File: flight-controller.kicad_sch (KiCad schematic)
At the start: 13 parts, among them J1 Conn_02x10_Odd_Even, J2 Conn_02x08_Odd_Even, J3 Conn_02x17_Odd_Even, J4 Conn_02x15_Counter_Clockwise, J5 Conn_01x02, U3 ACS773LCB-100B-PFF-T

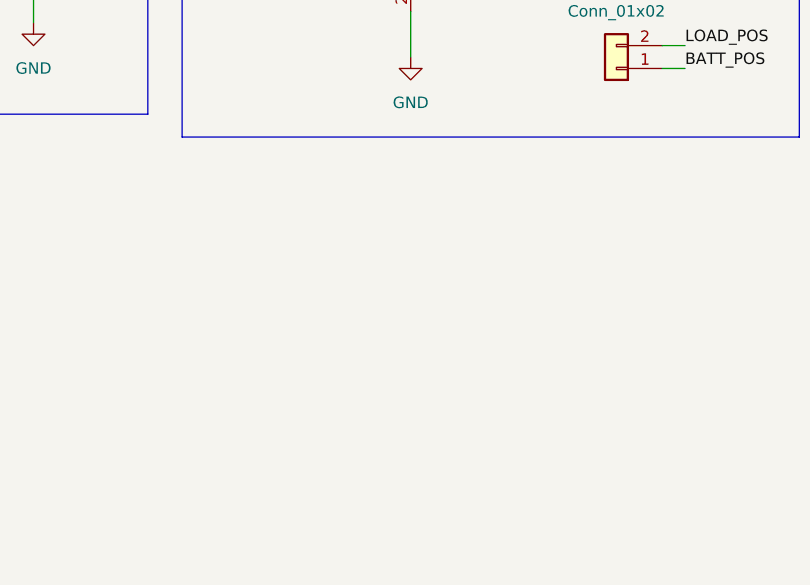
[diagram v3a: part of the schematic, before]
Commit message: feat: Added pinout of BN-088
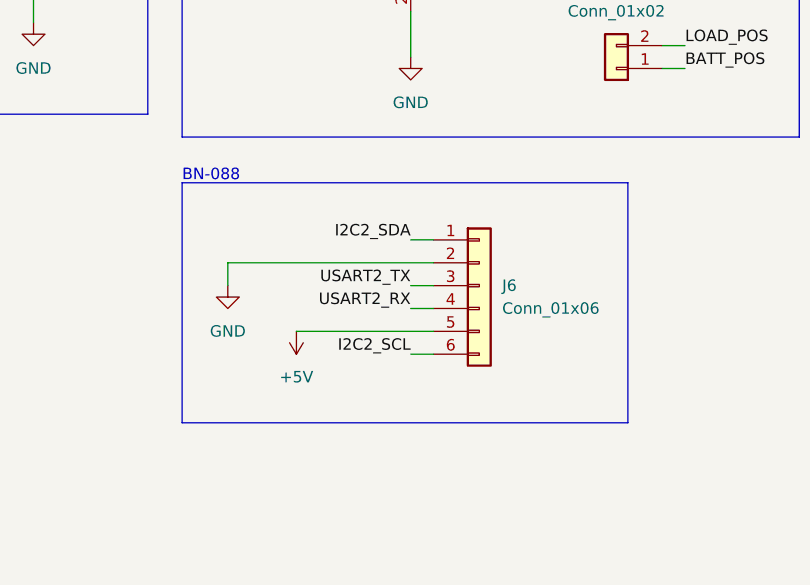
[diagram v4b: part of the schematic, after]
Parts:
- added J6: Conn_01x06, symbol Connector_Generic:Conn_01x06
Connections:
- net GND: now also J6.2 (Pin_2)
- new net +5V: J6.5 (Pin_5)
- new net I2C2_SCL: J6.6 (Pin_6)
- new net I2C2_SDA: J6.1 (Pin_1)
- new net USART2_RX: J6.4 (Pin_4)
- new net USART2_TX: J6.3 (Pin_3)
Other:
- note added: "BN-088"
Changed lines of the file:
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@@
+    (stroke (width 0) (type default))
+  )
+  (wire (pts (xy 219.71 88.9) (xy 222.25 88.9))
     (stroke (width 0) (type default))
   )
@@
     (stroke (width 0) (type default))
   )
+  (wire (pts (xy 219.71 93.98) (xy 222.25 93.98))
+    (stroke (width 0) (type default))
+  )
   (wire (pts (xy 148.59 48.26) (xy 153.67 48.26))
     (stroke (width 0) (type default))
@@
     (stroke (width 0) (type default))
   )
+  (wire (pts (xy 199.39 86.36) (xy 199.39 83.82))
+    (stroke (width 0) (type default))
+  )
   (wire (pts (xy 60.96 52.07) (xy 63.5 52.07))
     (stroke (width 0) (type default))
@@
     (stroke (width 0) (type default))
   )
+  (wire (pts (xy 207.01 91.44) (xy 222.25 91.44))
+    (stroke (width 0) (type default))
+  )
   (wire (pts (xy 63.5 52.07) (xy 63.5 54.61))
     (stroke (width 0) (type default))
@@
     (stroke (width 0) (type default))
   )
+  (wire (pts (xy 219.71 81.28) (xy 222.25 81.28))
+    (stroke (width 0) (type default))
+  )
   (wire (pts (xy 165.1 33.02) (xy 165.1 38.1))
     (stroke (width 0) (type default))
@@
     (stroke (width 0) (type default))
   )
+  (wire (pts (xy 199.39 83.82) (xy 222.25 83.82))
+    (stroke (width 0) (type default))
+  )
   (wire (pts (xy 93.98 49.53) (xy 93.98 53.34))
     (stroke (width 0) (type default))
@@
     (stroke (width 0) (type default))
   )
+  (wire (pts (xy 219.71 86.36) (xy 222.25 86.36))
+    (stroke (width 0) (type default))
+  )
   (wire (pts (xy 81.28 49.53) (xy 81.28 53.34))
     (stroke (width 0) (type default))
@@
     (fill (type none))
   )
+  (rectangle (start 194.31 74.93) (end 243.84 101.6)
+    (stroke (width 0) (type default))
+    (fill (type none))
+  )
   (text "ACS773" (at 194.31 24.13 0)
     (effects (font (size 1.27 1.27)) (justify left bottom))
@@
     (effects (font (size 1.27 1.27)) (justify left bottom))
   )
+  (text "BN-088" (at 194.31 74.93 0)
+    (effects (font (size 1.27 1.27)) (justify left bottom))
+  )
   (text "BMP390" (at 110.49 24.13 0)
     (effects (font (size 1.27 1.27)) (justify left bottom))
@@
     (effects (font (size 1.27 1.27)) (justify left bottom))
   )
+  (label "I2C2_SCL" (at 219.71 93.98 180) (fields_autoplaced)
+    (effects (font (size 1.27 1.27)) (justify right bottom))
+  )
   (label "LOAD_POS" (at 207.01 50.8 180) (fields_autoplaced)
     (effects (font (size 1.27 1.27)) (justify right bottom))
   )
+  (label "USART2_TX" (at 219.71 86.36 180) (fields_autoplaced)
+    (effects (font (size 1.27 1.27)) (justify right bottom))
+  )
   (label "SPI4_MISO" (at 125.73 43.18 180) (fields_autoplaced)
     (effects (font (size 1.27 1.27)) (justify right bottom))
@@
     (effects (font (size 1.27 1.27)) (justify right bottom))
   )
+  (label "USART2_RX" (at 219.71 88.9 180) (fields_autoplaced)
+    (effects (font (size 1.27 1.27)) (justify right bottom))
+  )
   (label "SPI1_CS_GYRO" (at 62.23 48.26 0) (fields_autoplaced)
     (effects (font (size 1.27 1.27)) (justify left bottom))
@@
   (label "SPI1_SCK" (at 62.23 40.64 0) (fields_autoplaced)
     (effects (font (size 1.27 1.27)) (justify left bottom))
+  )
+  (label "I2C2_SDA" (at 219.71 81.28 180) (fields_autoplaced)
+    (effects (font (size 1.27 1.27)) (justify right bottom))
   )
   (label "SPI1_MISO" (at 34.29 36.83 180) (fields_autoplaced)
@@
     )
   )
+  (symbol (lib_id "Connector_Generic:Conn_01x06") (at 227.33 86.36 0) (unit 1)
+    (in_bom yes) (on_board yes) (dnp no) (fields_autoplaced)
+    (property "Reference" "J6" (at 229.87 86.36 0)
+      (effects (font (size 1.27 1.27)) (justify left))
+    )
+    (property "Value" "Conn_01x06" (at 229.87 88.9 0)
+      (effects (font (size 1.27 1.27)) (justify left))
+    )
+    (property "Footprint" "" (at 227.33 86.36 0)
+      (effects (font (size 1.27 1.27)) hide)
+    )
+    (property "Datasheet" "~" (at 227.33 86.36 0)
+      (effects (font (size 1.27 1.27)) hide)
+    )
+    (pin "3")
+    (pin "4")
+    (pin "6")
+    (pin "2")
+    (pin "5")
+    (pin "1")
+    (instances
+      (project "flight-controller"
+        (path "/1e8bc6c3-9c25-4744-8bc3-112c39d50b38"
+          (reference "J6") (unit 1)
+        )
+      )
+    )
+  )
   (symbol (lib_id "power:GND") (at 177.8 57.15 0) (unit 1)
     (in_bom yes) (on_board yes) (dnp no) (fields_autoplaced)
@@
     )
   )
+  (symbol (lib_id "power:GND") (at 199.39 86.36 0) (unit 1)
+    (in_bom yes) (on_board yes) (dnp no) (fields_autoplaced)
+    (property "Reference" "#PWR016" (at 199.39 92.71 0)
+      (effects (font (size 1.27 1.27)) hide)
+    )
+    (property "Value" "GND" (at 199.39 91.44 0)
+      (effects (font (size 1.27 1.27)))
+    )
+    (property "Footprint" "" (at 199.39 86.36 0)
+      (effects (font (size 1.27 1.27)) hide)
+    )
+    (property "Datasheet" "" (at 199.39 86.36 0)
+      (effects (font (size 1.27 1.27)) hide)
+    )
+    (pin "1")
+    (instances
+      (project "flight-controller"
+        (path "/1e8bc6c3-9c25-4744-8bc3-112c39d50b38"
+          (reference "#PWR016") (unit 1)
+        )
+      )
+    )
+  )
   (symbol (lib_id "power:+3.3V") (at 213.36 35.56 90) (unit 1)
     (in_bom yes) (on_board yes) (dnp no) (fields_autoplaced)
@@
         )
       )
+    )
+  )
+  (symbol (lib_id "power:+5V") (at 207.01 91.44 180) (unit 1)
+    (in_bom yes) (on_board yes) (dnp no) (fields_autoplaced)
+    (property "Reference" "#PWR017" (at 207.01 87.63 0)
+      (effects (font (size 1.27 1.27)) hide)
+    )
+    (property "Value" "+5V" (at 207.01 96.52 0)
+      (effects (font (size 1.27 1.27)))
+    )
+    (property "Footprint" "" (at 207.01 91.44 0)
+      (effects (font (size 1.27 1.27)) hide)
+    )
+    (property "Datasheet" "" (at 207.01 91.44 0)
+      (effects (font (size 1.27 1.27)) hide)
+    )
+    (pin "1")
+    (instances
+      (project "flight-controller"
+        (path "/1e8bc6c3-9c25-4744-8bc3-112c39d50b38"
+          (reference "#PWR017") (unit 1)
+        )
+      )

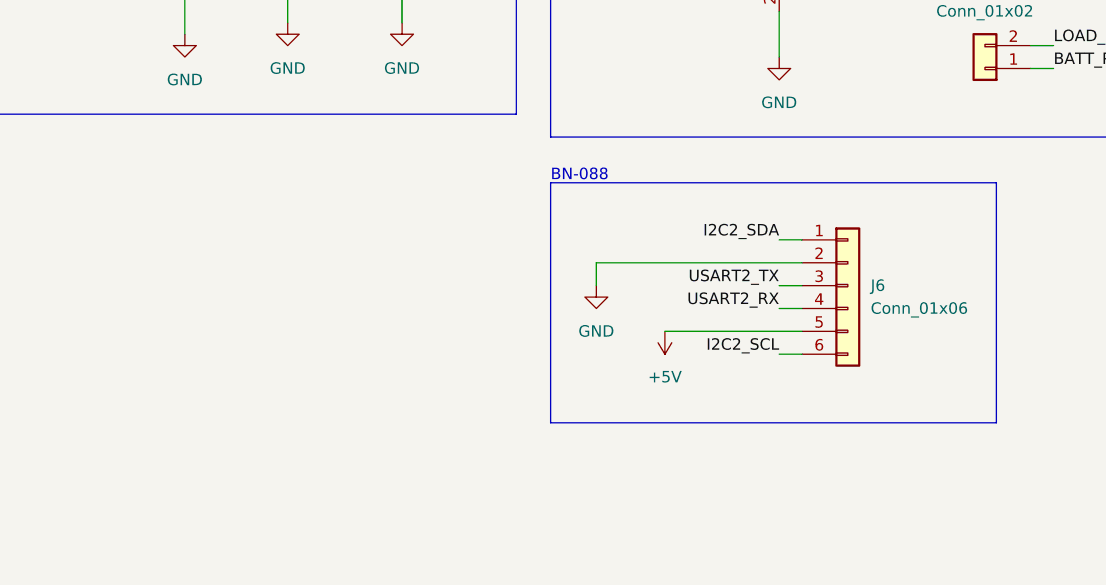
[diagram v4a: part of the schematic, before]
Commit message: feat: Added J_ESC_POWER pins for powering the board
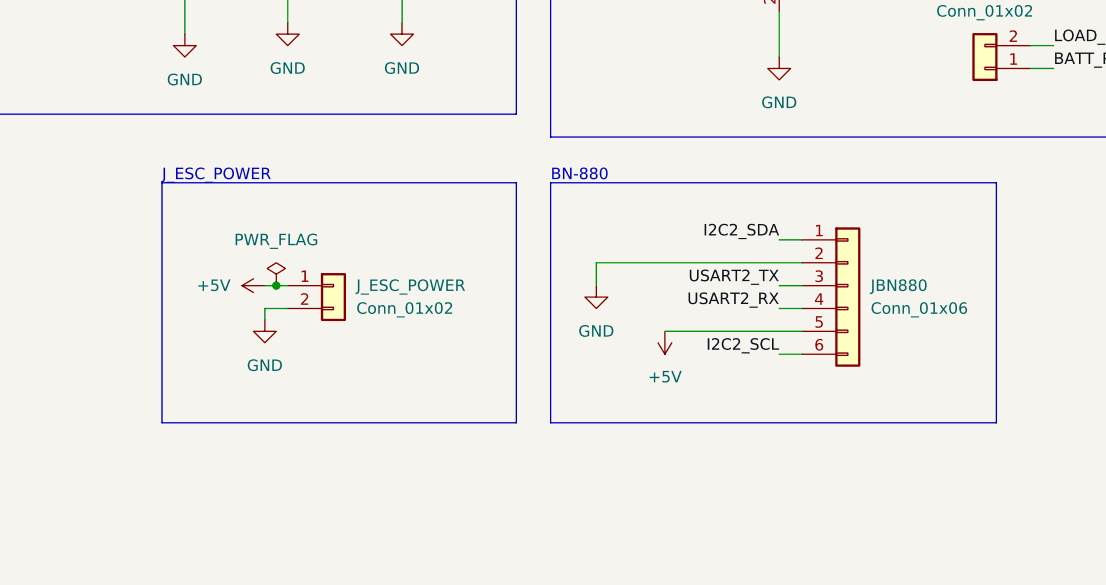
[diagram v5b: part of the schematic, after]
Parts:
- added J_ESC_POWER: Conn_01x02, symbol Connector_Generic:Conn_01x02
- renumbered J6 to JBN880
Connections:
- net +5V: now also J_ESC_POWER.1 (Pin_1)
- net GND: now also J_ESC_POWER.2 (Pin_2)
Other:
- note added: "BN-880"
- note added: "J_ESC_POWER"
- note removed: "BN-088"
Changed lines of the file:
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@@
   (junction (at 93.98 36.83) (diameter 0) (color 0 0 0 0)
+  )
+  (junction (at 163.83 86.36) (diameter 0) (color 0 0 0 0)
   )
   (junction (at 219.71 35.56) (diameter 0) (color 0 0 0 0)
@@
     (stroke (width 0) (type default))
   )
+  (wire (pts (xy 162.56 86.36) (xy 163.83 86.36))
+    (stroke (width 0) (type default))
+  )
   (wire (pts (xy 125.73 40.64) (xy 128.27 40.64))
     (stroke (width 0) (type default))
@@
     (stroke (width 0) (type default))
   )
+  (wire (pts (xy 163.83 86.36) (xy 165.1 86.36))
+    (stroke (width 0) (type default))
+  )
   (wire (pts (xy 247.65 62.23) (xy 250.19 62.23))
     (stroke (width 0) (type default))
@@
     (stroke (width 0) (type default))
   )
+  (wire (pts (xy 162.56 88.9) (xy 162.56 90.17))
+    (stroke (width 0) (type default))
+  )
+  (wire (pts (xy 165.1 88.9) (xy 162.56 88.9))
+    (stroke (width 0) (type default))
+  )
   (wire (pts (xy 93.98 31.75) (xy 93.98 36.83))
     (stroke (width 0) (type default))
@@
     (fill (type none))
   )
+  (rectangle (start 151.13 74.93) (end 190.5 101.6)
+    (stroke (width 0) (type default))
+    (fill (type none))
+  )
   (rectangle (start 110.49 24.13) (end 190.5 67.31)
     (stroke (width 0) (type default))
@@
     (effects (font (size 1.27 1.27)) (justify left bottom))
   )
+  (text "J_ESC_POWER" (at 151.13 74.93 0)
+    (effects (font (size 1.27 1.27)) (justify left bottom))
+  )
   (text "BMI088" (at 21.59 24.13 0)
     (effects (font (size 1.27 1.27)) (justify left bottom))
   )
-  (text "BN-088" (at 194.31 74.93 0)
+  (text "BN-880" (at 194.31 74.93 0)
     (effects (font (size 1.27 1.27)) (justify left bottom))
   )
@@
     )
   )
+  (symbol (lib_id "power:GND") (at 162.56 90.17 0) (unit 1)
+    (in_bom yes) (on_board yes) (dnp no) (fields_autoplaced)
+    (property "Reference" "#PWR018" (at 162.56 96.52 0)
+      (effects (font (size 1.27 1.27)) hide)
+    )
+    (property "Value" "GND" (at 162.56 95.25 0)
+      (effects (font (size 1.27 1.27)))
+    )
+    (property "Footprint" "" (at 162.56 90.17 0)
+      (effects (font (size 1.27 1.27)) hide)
+    )
+    (property "Datasheet" "" (at 162.56 90.17 0)
+      (effects (font (size 1.27 1.27)) hide)
+    )
+    (pin "1")
+    (instances
+      (project "flight-controller"
+        (path "/1e8bc6c3-9c25-4744-8bc3-112c39d50b38"
+          (reference "#PWR018") (unit 1)
+        )
+      )
+    )
+  )
   (symbol (lib_id "power:GND") (at 219.71 60.96 0) (unit 1)
     (in_bom yes) (on_board yes) (dnp no) (fields_autoplaced)
@@
   (symbol (lib_id "Connector_Generic:Conn_01x06") (at 227.33 86.36 0) (unit 1)
     (in_bom yes) (on_board yes) (dnp no) (fields_autoplaced)
-    (property "Reference" "J6" (at 229.87 86.36 0)
+    (property "Reference" "JBN880" (at 229.87 86.36 0)
       (effects (font (size 1.27 1.27)) (justify left))
     )
@@
       (project "flight-controller"
         (path "/1e8bc6c3-9c25-4744-8bc3-112c39d50b38"
-          (reference "J6") (unit 1)
+          (reference "JBN880") (unit 1)
         )
       )
@@
     )
   )
+  (symbol (lib_id "power:PWR_FLAG") (at 163.83 86.36 0) (unit 1)
+    (in_bom yes) (on_board yes) (dnp no) (fields_autoplaced)
+    (property "Reference" "#FLG01" (at 163.83 84.455 0)
+      (effects (font (size 1.27 1.27)) hide)
+    )
+    (property "Value" "PWR_FLAG" (at 163.83 81.28 0)
+      (effects (font (size 1.27 1.27)))
+    )
+    (property "Footprint" "" (at 163.83 86.36 0)
+      (effects (font (size 1.27 1.27)) hide)
+    )
+    (property "Datasheet" "~" (at 163.83 86.36 0)
+      (effects (font (size 1.27 1.27)) hide)
+    )
+    (pin "1")
+    (instances
+      (project "flight-controller"
+        (path "/1e8bc6c3-9c25-4744-8bc3-112c39d50b38"
+          (reference "#FLG01") (unit 1)
+        )
+      )
+    )
+  )
   (symbol (lib_id "power:+3.3V") (at 165.1 33.02 0) (unit 1)
     (in_bom yes) (on_board yes) (dnp no) (fields_autoplaced)
@@
     )
   )
+  (symbol (lib_id "power:+5V") (at 162.56 86.36 90) (unit 1)
+    (in_bom yes) (on_board yes) (dnp no) (fields_autoplaced)
+    (property "Reference" "#PWR019" (at 166.37 86.36 0)
+      (effects (font (size 1.27 1.27)) hide)
+    )
+    (property "Value" "+5V" (at 158.75 86.36 90)
+      (effects (font (size 1.27 1.27)) (justify left))
+    )
+    (property "Footprint" "" (at 162.56 86.36 0)
+      (effects (font (size 1.27 1.27)) hide)
+    )
+    (property "Datasheet" "" (at 162.56 86.36 0)
+      (effects (font (size 1.27 1.27)) hide)
+    )
+    (pin "1")
+    (instances
+      (project "flight-controller"
+        (path "/1e8bc6c3-9c25-4744-8bc3-112c39d50b38"
+          (reference "#PWR019") (unit 1)
+        )
+      )
+    )
+  )
   (symbol (lib_id "power:+3.3V") (at 177.8 33.02 0) (unit 1)
     (in_bom yes) (on_board yes) (dnp no) (fields_autoplaced)
@@
         )
       )
+    )
+  )
+  (symbol (lib_id "Connector_Generic:Conn_01x02") (at 170.18 86.36 0) (unit 1)
+    (in_bom yes) (on_board yes) (dnp no) (fields_autoplaced)
+    (property "Reference" "J_ESC_POWER" (at 172.72 86.36 0)
+      (effects (font (size 1.27 1.27)) (justify left))
+    )
+    (property "Value" "Conn_01x02" (at 172.72 88.9 0)
+      (effects (font (size 1.27 1.27)) (justify left))
+    )
+    (property "Footprint" "" (at 170.18 86.36 0)
+      (effects (font (size 1.27 1.27)) hide)
+    )
+    (property "Datasheet" "~" (at 170.18 86.36 0)
+      (effects (font (size 1.27 1.27)) hide)
+    )
+    (pin "2")
+    (pin "1")
+    (instances
+      (project "flight-controller"
+        (path "/1e8bc6c3-9c25-4744-8bc3-112c39d50b38"
+          (reference "J_ESC_POWER") (unit 1)
+        )
+      )
